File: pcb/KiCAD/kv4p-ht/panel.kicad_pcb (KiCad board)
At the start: 4 copper layers, 87.2 x 96.6 mm, 172 parts, among them J1 Antenna, J2 SMA, J4 SAO v.69bis, J5 USB-C Socket, J6 GPIO Header, Q1 SS8050, Q2 SS8050, Q3 AO3400A, SW1 PTT, SW2 PTT, SW3 Reset, SW4 Program, U1 DRA/SA818, U2 AZ1117H-3.3TRG1, U4 CP2102N-A02-GQFN24, U5 ESP32-WROOM-32E

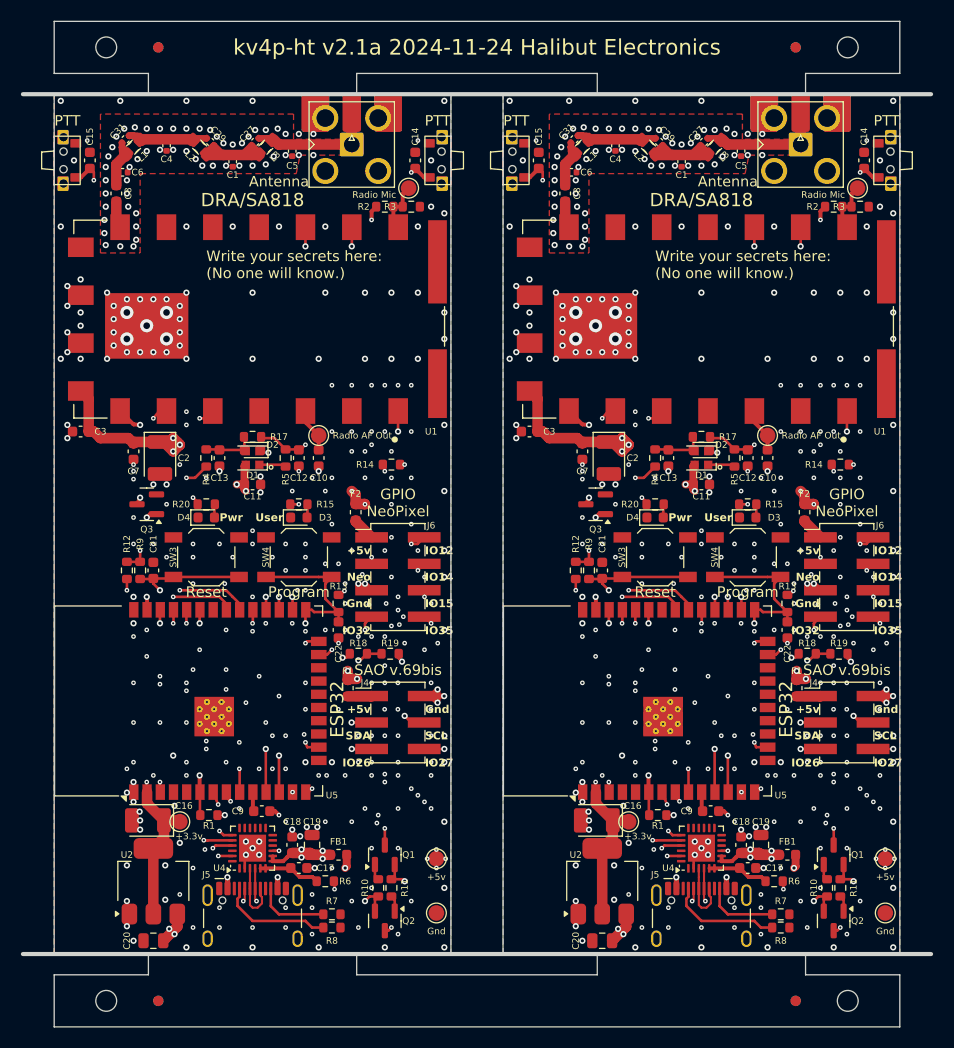
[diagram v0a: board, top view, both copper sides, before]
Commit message: Panelized for JLCPCB production. (They need 70x70mm.) #88
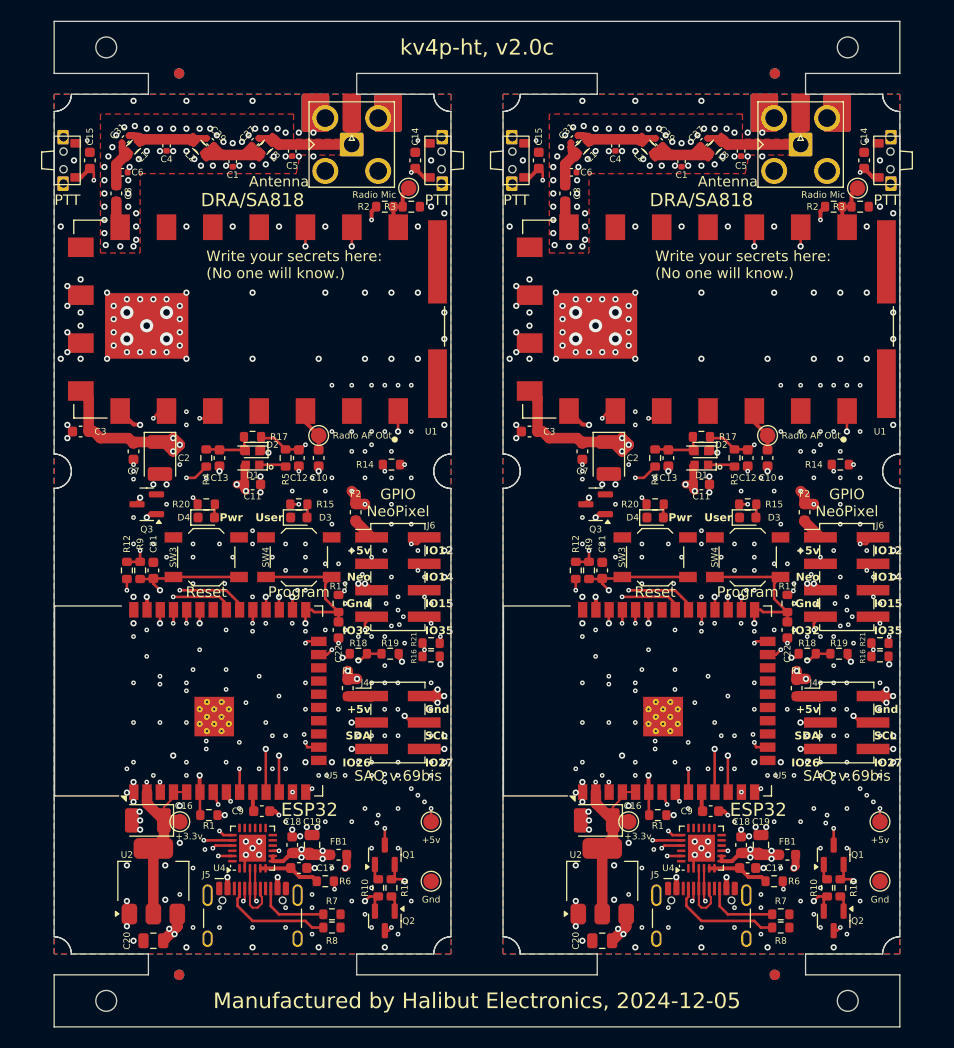
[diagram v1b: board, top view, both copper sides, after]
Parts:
- removed the TP1 at (187.7, 100.4)
- removed the TP1 at (144.6, 100.4)
- removed the TP3 at (187.7, 105.6)
- removed the TP3 at (144.6, 105.6)
- added R16: 100k, Resistor_SMD:R_0603_1608Metric, F.Cu at (144.1, 79.7)
- added R16: 100k, Resistor_SMD:R_0603_1608Metric, F.Cu at (187.2, 79.7)
- added R21: 100k, Resistor_SMD:R_0603_1608Metric, F.Cu at (144.1, 81.0)
- added R21: 100k, Resistor_SMD:R_0603_1608Metric, F.Cu at (187.2, 81.0)
- added TP1: +5v, TestPoint:TestPoint_Pad_D1.5mm, F.Cu at (144.1, 96.9)
- added TP1: +5v, TestPoint:TestPoint_Pad_D1.5mm, F.Cu at (187.2, 96.9)
- added TP3: Gnd, TestPoint:TestPoint_Pad_D1.5mm, F.Cu at (187.2, 102.6)
- added TP3: Gnd, TestPoint:TestPoint_Pad_D1.5mm, F.Cu at (144.1, 102.6)
- moved KiKit_FID_B_3 3.20 mm to (119.9, 111.6)
- moved KiKit_FID_T_3 3.20 mm to (119.9, 111.6)
- moved KiKit_FID_B_4 3.20 mm to (177.1, 111.6)
- moved KiKit_FID_T_4 3.20 mm to (177.1, 111.6)
- moved KiKit_FID_B_1 3.20 mm to (119.9, 25.0)
- moved KiKit_FID_T_1 3.20 mm to (119.9, 25.0)
- moved KiKit_FID_B_2 3.20 mm to (177.1, 25.0)
- moved KiKit_FID_T_2 3.20 mm to (177.1, 25.0)
- turned R6 to 180 degrees (x2)
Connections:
- U5 pad 4: Board_1-GND -> Board_1-+3.3V
- U5 pad 5: Board_1-GND -> Board_1-+3.3V
- U5 pad 4: Board_0-GND -> Board_0-+3.3V
- U5 pad 5: Board_0-GND -> Board_0-+3.3V
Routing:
- net Board_1-+3.3V: track 86.7 -> 91.1 mm
- net Board_0-+3.3V: track 86.7 -> 91.1 mm
- net Board_0-/GPIO15: track 16.1 -> 17.5 mm
- net Board_1-/GPIO15: track 16.1 -> 17.5 mm
- net Board_1-+5V: track 37.5 -> 38.7 mm, vias 165 -> 162
- net Board_0-+5V: track 37.5 -> 38.7 mm, vias 165 -> 162
- net Board_1-GND: vias 191 -> 185
- net Board_0-GND: vias 191 -> 185
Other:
- board size 87.2 x 96.6 mm -> 81.2 x 96.6 mm
- board text added: "Manufactured by Halibut Electronics, 2024-12-05"
- board text added: "kv4p HT, v2.0c 2024-12-05 VanceVagell v2 hardware by @SmittyHalibut"
- board text added: "kv4p-ht, v2.0c"
- board text removed: "kv4p HT, v2.1a 2024-11-26 VanceVagell v2 hardware by @SmittyHalibut"
- board text removed: "kv4p-ht v2.1a 2024-11-24 Halibut Electronics"

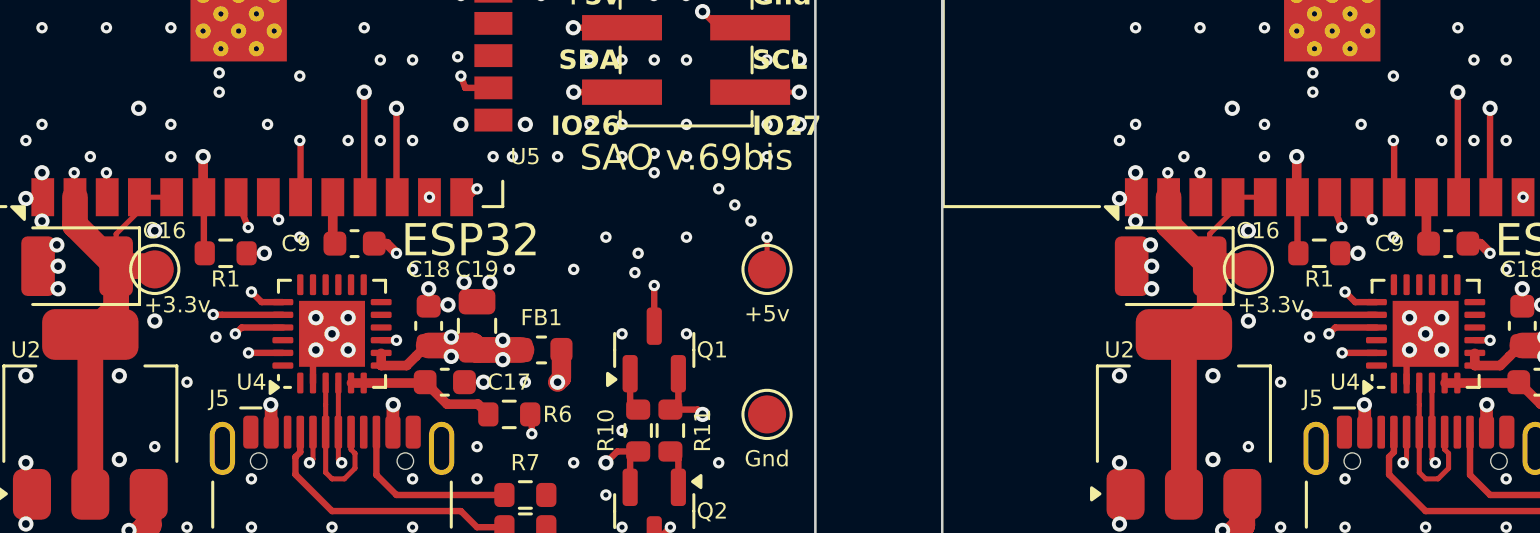
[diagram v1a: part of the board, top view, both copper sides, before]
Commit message: Thanks to @jh4vsm for finding this bug.  https://github.com/VanceVagell/kv4p-ht/pull/129#issuecomment-2522023437 #88 #129
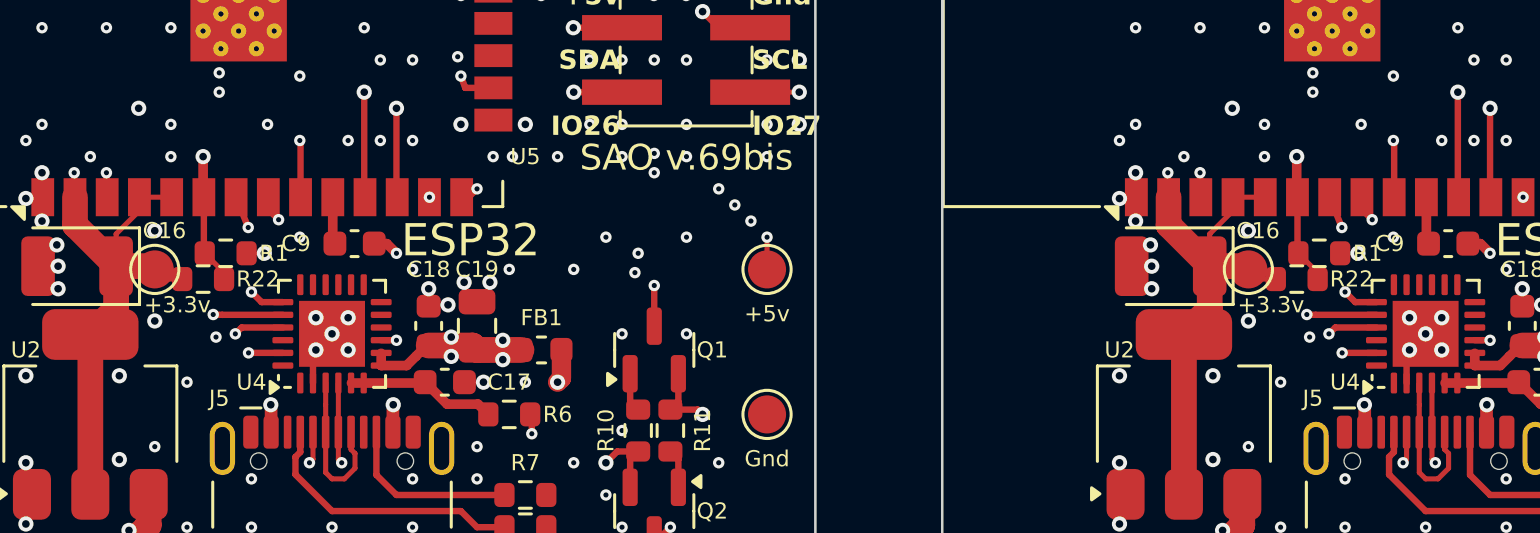
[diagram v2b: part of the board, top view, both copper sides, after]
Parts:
- added R22: 47k, Resistor_SMD:R_0603_1608Metric, F.Cu at (121.9, 97.2)
- added R22: 47k, Resistor_SMD:R_0603_1608Metric, F.Cu at (165.0, 97.2)
- U5 (x2): value ESP32-WROOM-32E -> ESP32-WROOM-32E-N4
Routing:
- net Board_1-Net-(U5-IO34): track 44.9 -> 46.2 mm
- net Board_0-Net-(U5-IO34): track 44.9 -> 46.2 mm
- net Board_1-+3.3V: track 91.1 -> 92.4 mm
- net Board_0-+3.3V: track 91.1 -> 92.4 mm
